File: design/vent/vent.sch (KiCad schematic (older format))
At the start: 19 parts, among them J10 CS_TEST, J2 OSTYK22102030, J3 SDA_TEST, J4 RX_TEST, J5 TX_TEST, J6 SCL_TEST, J7 SCK_TEST, J8 MISO_TEST, J9 MOSI_TEST

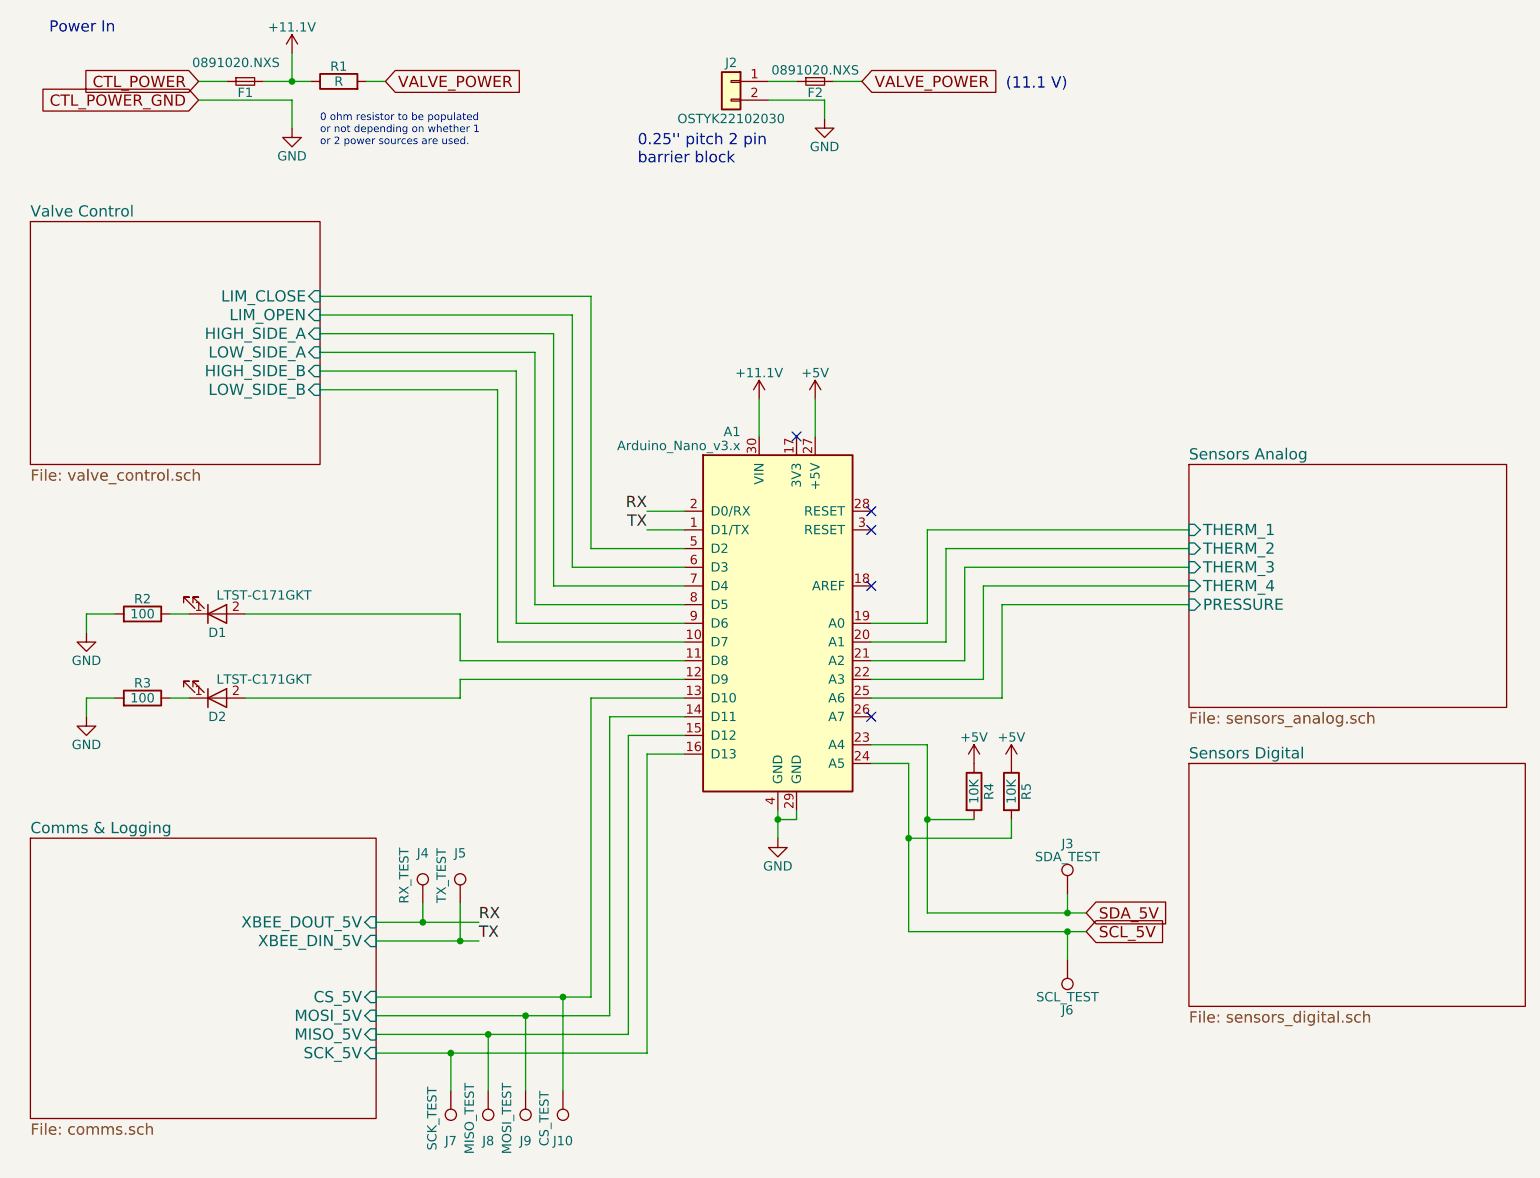
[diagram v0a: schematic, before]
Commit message: Vent & Injector Board Layout
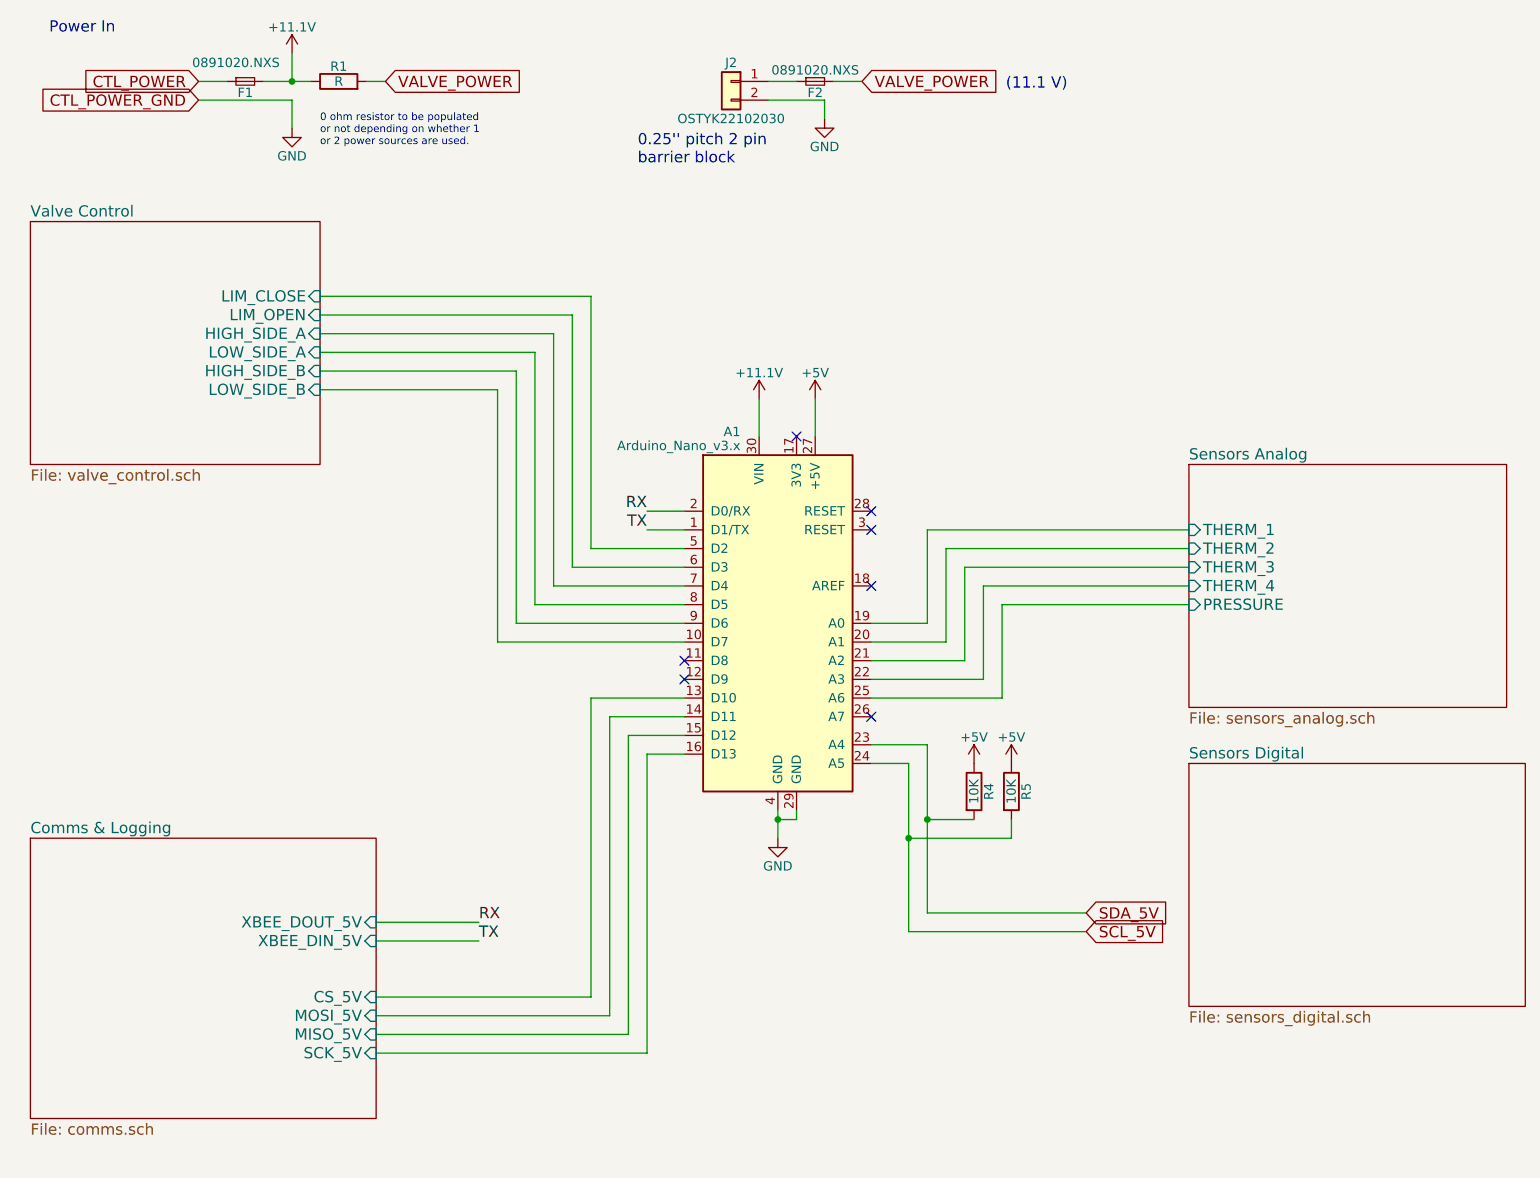
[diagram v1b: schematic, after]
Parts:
- removed D1, D2: LTST-C171GKT, LEDs:LED_0805_HandSoldering, symbol LED
- removed J10: CS_TEST, TestPoint:TestPoint_Pad_D2.0mm, symbol TEST_1P
- removed J3: SDA_TEST, TestPoint:TestPoint_Pad_D2.0mm, symbol TEST_1P
- removed J4: RX_TEST, TestPoint:TestPoint_Pad_D2.0mm, symbol TEST_1P
- removed J5: TX_TEST, TestPoint:TestPoint_Pad_D2.0mm, symbol TEST_1P
- removed J6: SCL_TEST, TestPoint:TestPoint_Pad_D2.0mm, symbol TEST_1P
- removed J7: SCK_TEST, TestPoint:TestPoint_Pad_D2.0mm, symbol TEST_1P
- removed J8: MISO_TEST, TestPoint:TestPoint_Pad_D2.0mm, symbol TEST_1P
- removed J9: MOSI_TEST, TestPoint:TestPoint_Pad_D2.0mm, symbol TEST_1P
- removed R2, R3: 100, Resistors_SMD:R_0805_HandSoldering, symbol R
- A1: footprint Modules:Arduino_Nano -> Module:Arduino_Nano
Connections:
- no-connect marks 5 -> 7
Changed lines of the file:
@@
 F 0 "A1" H 5400 5275 50  0000 R CNN
 F 1 "Arduino_Nano_v3.x" H 5400 5200 50  0000 R CNN
-F 2 "Modules:Arduino_Nano" H 5750 3300 50  0001 L CNN
+F 2 "Module:Arduino_Nano" H 5750 3300 50  0001 L CNN
 F 3 "" H 5600 3250 50  0001 C CNN
 	1    5600 4250
@@
 	1    0    0    -1
 $EndComp
-$Comp
-L TEST_1P J3
-U 1 1 5AE89716
-P 7150 5700
-F 0 "J3" H 7150 5970 50  0000 C CNN
-F 1 "SDA_TEST" H 7150 5900 50  0000 C CNN
-F 2 "TestPoint:TestPoint_Pad_D2.0mm" H 7350 5700 50  0001 C CNN
-F 3 "" H 7350 5700 50  0001 C CNN
-	1    7150 5700
-	1    0    0    -1
-$EndComp
-$Comp
-L TEST_1P J6
-U 1 1 5AE8977F
-P 7150 6050
-F 0 "J6" H 7150 6320 50  0000 C CNN
-F 1 "SCL_TEST" H 7150 6250 50  0000 C CNN
-F 2 "TestPoint:TestPoint_Pad_D2.0mm" H 7350 6050 50  0001 C CNN
-F 3 "" H 7350 6050 50  0001 C CNN
-	1    7150 6050
-	-1   0    0    1
-$EndComp
 Text Label 4000 5850 0    60   ~ 0
 RX
@@
 TX
 $Comp
-L TEST_1P J7
-U 1 1 5AE8F8D8
-P 3850 6750
-F 0 "J7" H 3850 7020 50  0000 C CNN
-F 1 "SCK_TEST" V 3950 6900 50  0000 C CNN
-F 2 "TestPoint:TestPoint_Pad_D2.0mm" H 4050 6750 50  0001 C CNN
-F 3 "" H 4050 6750 50  0001 C CNN
-	1    3850 6750
-	-1   0    0    1
-$EndComp
-$Comp
-L TEST_1P J8
-U 1 1 5AE8FB6E
-P 4050 6750
-F 0 "J8" H 4050 7020 50  0000 C CNN
-F 1 "MISO_TEST" V 4150 6900 50  0000 C CNN
-F 2 "TestPoint:TestPoint_Pad_D2.0mm" H 4250 6750 50  0001 C CNN
-F 3 "" H 4250 6750 50  0001 C CNN
-	1    4050 6750
-	-1   0    0    1
-$EndComp
-$Comp
-L TEST_1P J9
-U 1 1 5AE8FBFF
-P 4250 6750
-F 0 "J9" H 4250 7020 50  0000 C CNN
-F 1 "MOSI_TEST" V 4350 6900 50  0000 C CNN
-F 2 "TestPoint:TestPoint_Pad_D2.0mm" H 4450 6750 50  0001 C CNN
-F 3 "" H 4450 6750 50  0001 C CNN
-	1    4250 6750
-	-1   0    0    1
-$EndComp
-$Comp
-L TEST_1P J10
-U 1 1 5AE8FC91
-P 4450 6750
-F 0 "J10" H 4450 7020 50  0000 C CNN
-F 1 "CS_TEST" V 4550 6900 50  0000 C CNN
-F 2 "TestPoint:TestPoint_Pad_D2.0mm" H 4650 6750 50  0001 C CNN
-F 3 "" H 4650 6750 50  0001 C CNN
-	1    4450 6750
-	-1   0    0    1
-$EndComp
-$Comp
-L TEST_1P J4
-U 1 1 5AE91133
-P 3700 5750
-F 0 "J4" H 3700 6020 50  0000 C CNN
-F 1 "RX_TEST" V 3600 5900 50  0000 C CNN
-F 2 "TestPoint:TestPoint_Pad_D2.0mm" H 3900 5750 50  0001 C CNN
-F 3 "" H 3900 5750 50  0001 C CNN
-	1    3700 5750
-	1    0    0    -1
-$EndComp
-$Comp
-L TEST_1P J5
-U 1 1 5AE91C4F
-P 3900 5750
-F 0 "J5" H 3900 6020 50  0000 C CNN
-F 1 "TX_TEST" V 3800 5900 50  0000 C CNN
-F 2 "TestPoint:TestPoint_Pad_D2.0mm" H 4100 5750 50  0001 C CNN
-F 3 "" H 4100 5750 50  0001 C CNN
-	1    3900 5750
-	1    0    0    -1
-$EndComp
-$Comp
 L Fuse_Small F1
 U 1 1 5AE9CD78
@@
 Connection ~ 6300 5400
 Wire Wire Line
-	7150 6050 7150 5900
-Wire Wire Line
-	7150 5800 7150 5700
-Wire Wire Line
 	6100 4250 6400 4250
 Wire Wire Line
@@
 	4600 4650 5100 4650
 Wire Wire Line
-	3850 6750 3850 6550
-Connection ~ 3850 6550
-Wire Wire Line
-	4050 6750 4050 6450
-Connection ~ 4050 6450
-Wire Wire Line
-	4250 6750 4250 6350
-Connection ~ 4250 6350
-Wire Wire Line
-	4450 6750 4450 6250
-Connection ~ 4450 6250
-Wire Wire Line
-	3700 5750 3700 5850
-Connection ~ 3700 5850
-Wire Wire Line
-	3900 5750 3900 5950
-Connection ~ 3900 5950
-Wire Wire Line
 	2500 1350 2650 1350
 Wire Wire Line
@@
 Wire Wire Line
 	4100 4350 5100 4350
-$Comp
-L LED D1
-U 1 1 5AEE352A
-P 2600 4200
-F 0 "D1" H 2600 4300 50  0000 C CNN
-F 1 "LTST-C171GKT" H 2850 4100 50  0000 C CNN
-F 2 "LEDs:LED_0805_HandSoldering" H 2600 4200 50  0001 C CNN
-F 3 "" H 2600 4200 50  0001 C CNN
-	1    2600 4200
-	1    0    0    1
-$EndComp
-$Comp
-L R R2
-U 1 1 5AEE369D
-P 2200 4200
-F 0 "R2" V 2280 4200 50  0000 C CNN
-F 1 "100" V 2200 4200 50  0000 C CNN
-F 2 "Resistors_SMD:R_0805_HandSoldering" V 2130 4200 50  0001 C CNN
-F 3 "" H 2200 4200 50  0001 C CNN
-	1    2200 4200
-	0    1    -1   0
-$EndComp
-Wire Wire Line
-	2450 4200 2350 4200
-$Comp
-L GND #PWR08
-U 1 1 5AEE382E
-P 1900 4300
-F 0 "#PWR08" H 1900 4050 50  0001 C CNN
-F 1 "GND" H 1900 4150 50  0000 C CNN
-F 2 "" H 1900 4300 50  0001 C CNN
-F 3 "" H 1900 4300 50  0001 C CNN
-	1    1900 4300
-	1    0    0    -1
-$EndComp
-Wire Wire Line
-	1900 4300 1900 4200
-Wire Wire Line
-	1900 4200 2050 4200
-$Comp
-L LED D2
-U 1 1 5AEE463E
-P 2600 4650
-F 0 "D2" H 2600 4750 50  0000 C CNN
-F 1 "LTST-C171GKT" H 2850 4550 50  0000 C CNN
-F 2 "LEDs:LED_0805_HandSoldering" H 2600 4650 50  0001 C CNN
-F 3 "" H 2600 4650 50  0001 C CNN
-	1    2600 4650
-	1    0    0    1
-$EndComp
-$Comp
-L R R3
-U 1 1 5AEE4645
-P 2200 4650
-F 0 "R3" V 2280 4650 50  0000 C CNN
-F 1 "100" V 2200 4650 50  0000 C CNN
-F 2 "Resistors_SMD:R_0805_HandSoldering" V 2130 4650 50  0001 C CNN
-F 3 "" H 2200 4650 50  0001 C CNN
-	1    2200 4650
-	0    1    -1   0
-$EndComp
-Wire Wire Line
-	2450 4650 2350 4650
-$Comp
-L GND #PWR09
-U 1 1 5AEE464D
-P 1900 4750
-F 0 "#PWR09" H 1900 4500 50  0001 C CNN
-F 1 "GND" H 1900 4600 50  0000 C CNN
-F 2 "" H 1900 4750 50  0001 C CNN
-F 3 "" H 1900 4750 50  0001 C CNN
-	1    1900 4750
-	1    0    0    -1
-$EndComp
-Wire Wire Line
-	1900 4750 1900 4650
-Wire Wire Line
-	1900 4650 2050 4650
-Wire Wire Line
-	2750 4200 3900 4200
-Wire Wire Line
-	3900 4200 3900 4450
-Wire Wire Line
-	3900 4450 5100 4450
-Wire Wire Line
-	2750 4650 3900 4650
-Wire Wire Line
-	3900 4650 3900 4550
-Wire Wire Line
-	3900 4550 5100 4550
 $Comp
 L Conn_01x02 J2
@@
 $EndComp
 $Comp
-L GND #PWR010
+L GND #PWR08
 U 1 1 5AEFA08B
 P 5850 1550
-F 0 "#PWR010" H 5850 1300 50  0001 C CNN
+F 0 "#PWR08" H 5850 1300 50  0001 C CNN
 F 1 "GND" H 5850 1400 50  0000 C CNN
 F 2 "" H 5850 1550 50  0001 C CNN
@@
 Text GLabel 7250 5900 2    60   Input ~ 0
 SCL_5V
-Connection ~ 7150 5800
-Connection ~ 7150 5900
 Text Notes 4850 1800 0    60   ~ 0
 0.25'' pitch 2 pin\nbarrier block
+NoConn ~ 5100 4450
+NoConn ~ 5100 4550
 $EndSCHEMATC

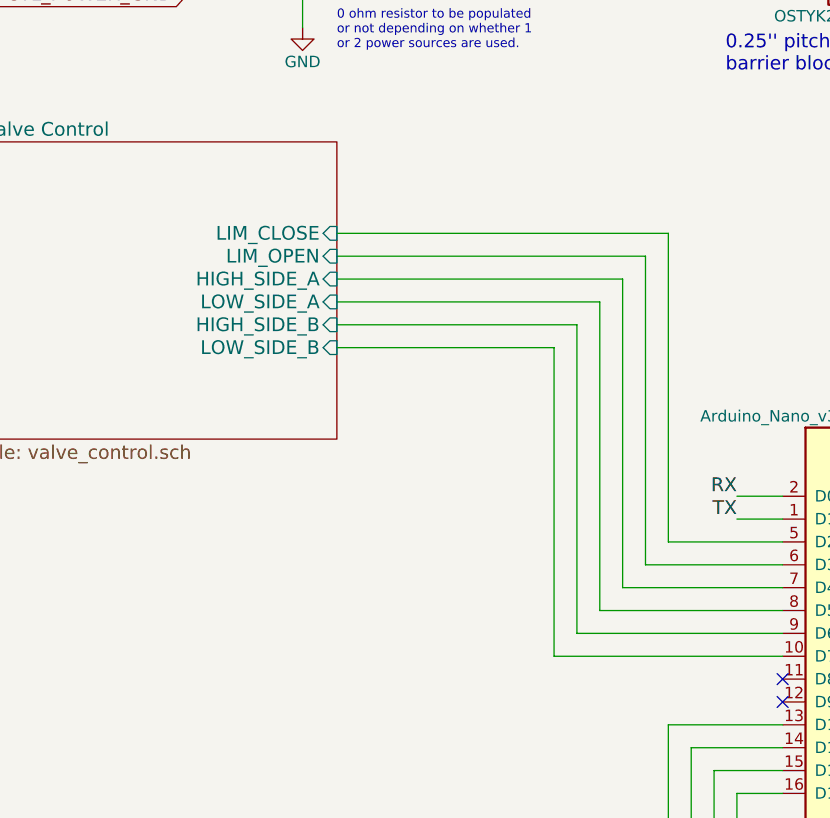
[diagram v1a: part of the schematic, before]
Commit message: Final vent/injector layout + routing
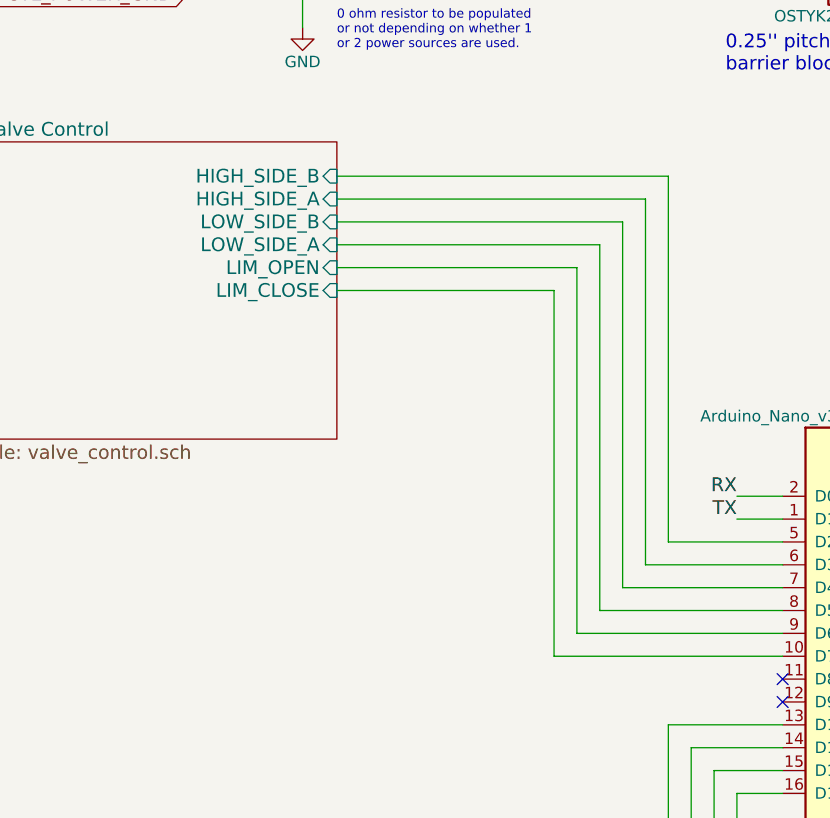
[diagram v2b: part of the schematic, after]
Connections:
- net Valve Control/HIGH_SIDE_A: now also A1.6 (D3); no longer A1.7 (D4)
- net Valve Control/HIGH_SIDE_B: now also A1.5 (D2); no longer A1.9 (D6)
- net Valve Control/LIM_CLOSE: now also A1.10 (D7); no longer A1.5 (D2)
- net Valve Control/LIM_OPEN: now also A1.9 (D6); no longer A1.6 (D3)
- net Valve Control/LOW_SIDE_B: now also A1.7 (D4); no longer A1.10 (D7)
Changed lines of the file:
@@
 F0 "Valve Control" 60
 F1 "valve_control.sch" 60
-F2 "LIM_OPEN" I R 3150 2600 60
-F3 "LIM_CLOSE" I R 3150 2500 60
-F4 "HIGH_SIDE_A" I R 3150 2700 60
-F5 "LOW_SIDE_A" I R 3150 2800 60
-F6 "HIGH_SIDE_B" I R 3150 2900 60
-F7 "LOW_SIDE_B" I R 3150 3000 60
+F2 "LIM_OPEN" I R 3150 2650 60
+F3 "LIM_CLOSE" I R 3150 2750 60
+F4 "HIGH_SIDE_A" I R 3150 2350 60
+F5 "LOW_SIDE_A" I R 3150 2550 60
+F6 "HIGH_SIDE_B" I R 3150 2250 60
+F7 "LOW_SIDE_B" I R 3150 2450 60
 $EndSheet
 $Comp
@@
 	2850 1350 3100 1350
 Wire Wire Line
-	3150 2500 4600 2500
-Wire Wire Line
-	4600 2500 4600 3850
+	4600 2250 4600 3850
 Wire Wire Line
 	4600 3850 5100 3850
 Wire Wire Line
-	3150 2600 4500 2600
-Wire Wire Line
-	4500 2600 4500 3950
+	4500 2350 4500 3950
 Wire Wire Line
 	4500 3950 5100 3950
 Wire Wire Line
-	3150 2700 4400 2700
-Wire Wire Line
-	4400 2700 4400 4050
+	4400 2450 4400 4050
 Wire Wire Line
 	4400 4050 5100 4050
 Wire Wire Line
-	3150 2800 4300 2800
-Wire Wire Line
-	4300 2800 4300 4150
+	4300 2550 4300 4150
 Wire Wire Line
 	4300 4150 5100 4150
 Wire Wire Line
-	3150 2900 4200 2900
-Wire Wire Line
-	4200 2900 4200 4250
+	4200 2650 4200 4250
 Wire Wire Line
 	4200 4250 5100 4250
 Wire Wire Line
-	3150 3000 4100 3000
-Wire Wire Line
-	4100 3000 4100 4350
+	4100 2750 4100 4350
 Wire Wire Line
 	4100 4350 5100 4350
@@
 NoConn ~ 5100 4450
 NoConn ~ 5100 4550
+Wire Wire Line
+	4600 2250 3150 2250
+Wire Wire Line
+	3150 2350 4500 2350
+Wire Wire Line
+	4400 2450 3150 2450
+Wire Wire Line
+	3150 2550 4300 2550
+Wire Wire Line
+	4200 2650 3150 2650
+Wire Wire Line
+	3150 2750 4100 2750
 $EndSCHEMATC
